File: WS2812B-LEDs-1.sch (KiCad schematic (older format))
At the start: 64 parts

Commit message: Getting lost in hirarchical schematic sheets...
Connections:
- net +5V renamed VCC

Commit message: Being creative...
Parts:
- C10, C11, C12, C13, C14, C15, C16, C17, C18, C19, C20, C21, C22, C23, C24, C25, C26, C27, C28, C29, C30, C31, C32, C33, C34, C35, C36, C5, C6, C7, C8, C9: footprint (none) -> my_parts:MADW__C0805
- LED1, LED10, LED11, LED12, LED13, LED14, LED15, LED16, LED17, LED18, LED19, LED2, LED20, LED21, LED22, LED23, LED24, LED25, LED26, LED27, LED28, LED29, LED3, LED30, LED31, LED32, LED4, LED5, LED6, LED7, LED8, LED9: footprint (none) -> WS2812B:WS2812B_data-bridgeable

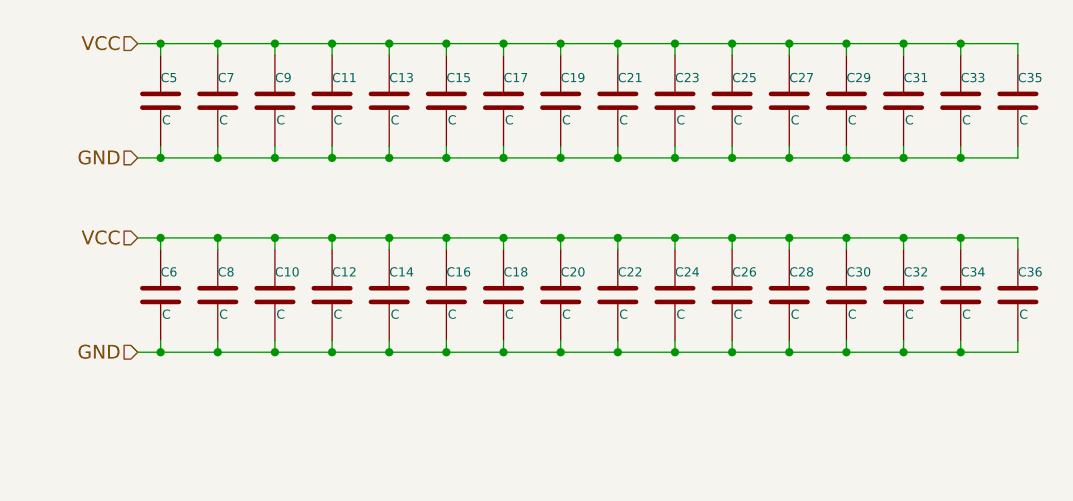
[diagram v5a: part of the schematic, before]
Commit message: Some cleanup. Still need to fix the power connector(s).
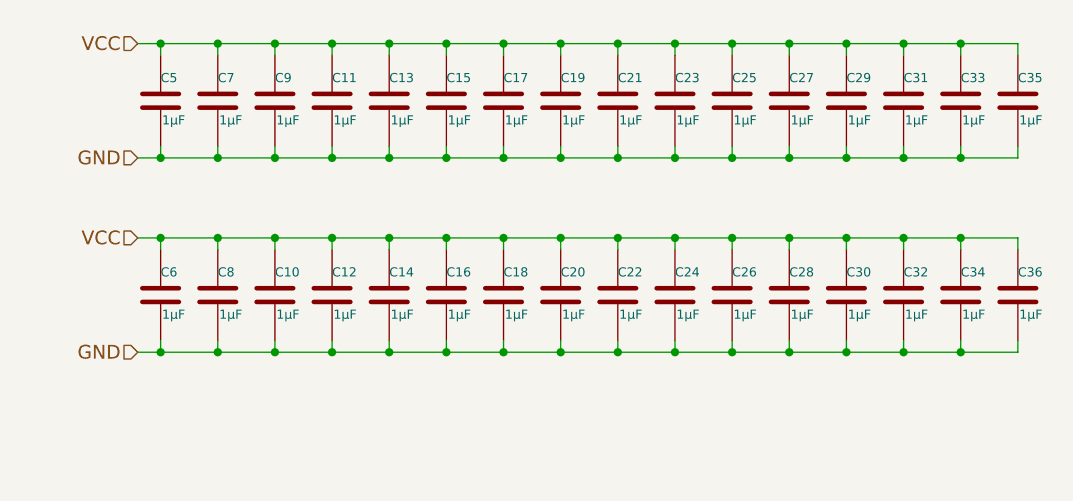
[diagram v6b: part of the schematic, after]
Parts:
- C10, C11, C12, C13, C14, C15, C16, C17, C18, C19, C20, C21, C22, C23, C24, C25, C26, C27, C28, C29, C30, C31, C32, C33, C34, C35, C36, C5, C6, C7, C8, C9: value C -> 1µF
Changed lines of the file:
@@
 P 7250 950
 F 0 "C5" H 7250 1050 40  0000 L CNN
-F 1 "C" H 7256 865 40  0000 L CNN
+F 1 "1µF" H 7256 865 40  0000 L CNN
 F 2 "my_parts:MADW__C0805" H 7288 800 30  0001 C CNN
 F 3 "" H 7250 950 60  0000 C CNN
@@
 P 7500 950
 F 0 "C7" H 7500 1050 40  0000 L CNN
-F 1 "C" H 7506 865 40  0000 L CNN
+F 1 "1µF" H 7506 865 40  0000 L CNN
 F 2 "my_parts:MADW__C0805" H 7538 800 30  0001 C CNN
 F 3 "" H 7500 950 60  0000 C CNN
@@
 P 7750 950
 F 0 "C9" H 7750 1050 40  0000 L CNN
-F 1 "C" H 7756 865 40  0000 L CNN
+F 1 "1µF" H 7756 865 40  0000 L CNN
 F 2 "my_parts:MADW__C0805" H 7788 800 30  0001 C CNN
 F 3 "" H 7750 950 60  0000 C CNN
@@
 P 8000 950
 F 0 "C11" H 8000 1050 40  0000 L CNN
-F 1 "C" H 8006 865 40  0000 L CNN
+F 1 "1µF" H 8006 865 40  0000 L CNN
 F 2 "my_parts:MADW__C0805" H 8038 800 30  0001 C CNN
 F 3 "" H 8000 950 60  0000 C CNN
@@
 P 8250 950
 F 0 "C13" H 8250 1050 40  0000 L CNN
-F 1 "C" H 8256 865 40  0000 L CNN
+F 1 "1µF" H 8256 865 40  0000 L CNN
 F 2 "my_parts:MADW__C0805" H 8288 800 30  0001 C CNN
 F 3 "" H 8250 950 60  0000 C CNN
@@
 P 8500 950
 F 0 "C15" H 8500 1050 40  0000 L CNN
-F 1 "C" H 8506 865 40  0000 L CNN
+F 1 "1µF" H 8506 865 40  0000 L CNN
 F 2 "my_parts:MADW__C0805" H 8538 800 30  0001 C CNN
 F 3 "" H 8500 950 60  0000 C CNN
@@
 P 8750 950
 F 0 "C17" H 8750 1050 40  0000 L CNN
-F 1 "C" H 8756 865 40  0000 L CNN
+F 1 "1µF" H 8756 865 40  0000 L CNN
 F 2 "my_parts:MADW__C0805" H 8788 800 30  0001 C CNN
 F 3 "" H 8750 950 60  0000 C CNN
@@
 P 9000 950
 F 0 "C19" H 9000 1050 40  0000 L CNN
-F 1 "C" H 9006 865 40  0000 L CNN
+F 1 "1µF" H 9006 865 40  0000 L CNN
 F 2 "my_parts:MADW__C0805" H 9038 800 30  0001 C CNN
 F 3 "" H 9000 950 60  0000 C CNN
@@
 P 9250 950
 F 0 "C21" H 9250 1050 40  0000 L CNN
-F 1 "C" H 9256 865 40  0000 L CNN
+F 1 "1µF" H 9256 865 40  0000 L CNN
 F 2 "my_parts:MADW__C0805" H 9288 800 30  0001 C CNN
 F 3 "" H 9250 950 60  0000 C CNN
@@
 P 9500 950
 F 0 "C23" H 9500 1050 40  0000 L CNN
-F 1 "C" H 9506 865 40  0000 L CNN
+F 1 "1µF" H 9506 865 40  0000 L CNN
 F 2 "my_parts:MADW__C0805" H 9538 800 30  0001 C CNN
 F 3 "" H 9500 950 60  0000 C CNN
@@
 P 9750 950
 F 0 "C25" H 9750 1050 40  0000 L CNN
-F 1 "C" H 9756 865 40  0000 L CNN
+F 1 "1µF" H 9756 865 40  0000 L CNN
 F 2 "my_parts:MADW__C0805" H 9788 800 30  0001 C CNN
 F 3 "" H 9750 950 60  0000 C CNN
@@
 P 10000 950
 F 0 "C27" H 10000 1050 40  0000 L CNN
-F 1 "C" H 10006 865 40  0000 L CNN
+F 1 "1µF" H 10006 865 40  0000 L CNN
 F 2 "my_parts:MADW__C0805" H 10038 800 30  0001 C CNN
 F 3 "" H 10000 950 60  0000 C CNN
@@
 P 10250 950
 F 0 "C29" H 10250 1050 40  0000 L CNN
-F 1 "C" H 10256 865 40  0000 L CNN
+F 1 "1µF" H 10256 865 40  0000 L CNN
 F 2 "my_parts:MADW__C0805" H 10288 800 30  0001 C CNN
 F 3 "" H 10250 950 60  0000 C CNN
@@
 P 10500 950
 F 0 "C31" H 10500 1050 40  0000 L CNN
-F 1 "C" H 10506 865 40  0000 L CNN
+F 1 "1µF" H 10506 865 40  0000 L CNN
 F 2 "my_parts:MADW__C0805" H 10538 800 30  0001 C CNN
 F 3 "" H 10500 950 60  0000 C CNN
@@
 P 10750 950
 F 0 "C33" H 10750 1050 40  0000 L CNN
-F 1 "C" H 10756 865 40  0000 L CNN
+F 1 "1µF" H 10756 865 40  0000 L CNN
 F 2 "my_parts:MADW__C0805" H 10788 800 30  0001 C CNN
 F 3 "" H 10750 950 60  0000 C CNN
@@
 P 11000 950
 F 0 "C35" H 11000 1050 40  0000 L CNN
-F 1 "C" H 11006 865 40  0000 L CNN
+F 1 "1µF" H 11006 865 40  0000 L CNN
 F 2 "my_parts:MADW__C0805" H 11038 800 30  0001 C CNN
 F 3 "" H 11000 950 60  0000 C CNN
@@
 P 7250 1800
 F 0 "C6" H 7250 1900 40  0000 L CNN
-F 1 "C" H 7256 1715 40  0000 L CNN
+F 1 "1µF" H 7256 1715 40  0000 L CNN
 F 2 "my_parts:MADW__C0805" H 7288 1650 30  0001 C CNN
 F 3 "" H 7250 1800 60  0000 C CNN
@@
 P 7500 1800
 F 0 "C8" H 7500 1900 40  0000 L CNN
-F 1 "C" H 7506 1715 40  0000 L CNN
+F 1 "1µF" H 7506 1715 40  0000 L CNN
 F 2 "my_parts:MADW__C0805" H 7538 1650 30  0001 C CNN
 F 3 "" H 7500 1800 60  0000 C CNN
@@
 P 7750 1800
 F 0 "C10" H 7750 1900 40  0000 L CNN
-F 1 "C" H 7756 1715 40  0000 L CNN
+F 1 "1µF" H 7756 1715 40  0000 L CNN
 F 2 "my_parts:MADW__C0805" H 7788 1650 30  0001 C CNN
 F 3 "" H 7750 1800 60  0000 C CNN
@@
 P 8000 1800
 F 0 "C12" H 8000 1900 40  0000 L CNN
-F 1 "C" H 8006 1715 40  0000 L CNN
+F 1 "1µF" H 8006 1715 40  0000 L CNN
 F 2 "my_parts:MADW__C0805" H 8038 1650 30  0001 C CNN
 F 3 "" H 8000 1800 60  0000 C CNN
@@
 P 8250 1800
 F 0 "C14" H 8250 1900 40  0000 L CNN
-F 1 "C" H 8256 1715 40  0000 L CNN
+F 1 "1µF" H 8256 1715 40  0000 L CNN
 F 2 "my_parts:MADW__C0805" H 8288 1650 30  0001 C CNN
 F 3 "" H 8250 1800 60  0000 C CNN
@@
 P 8500 1800
 F 0 "C16" H 8500 1900 40  0000 L CNN
-F 1 "C" H 8506 1715 40  0000 L CNN
+F 1 "1µF" H 8506 1715 40  0000 L CNN
 F 2 "my_parts:MADW__C0805" H 8538 1650 30  0001 C CNN
 F 3 "" H 8500 1800 60  0000 C CNN
@@
 P 8750 1800
 F 0 "C18" H 8750 1900 40  0000 L CNN
-F 1 "C" H 8756 1715 40  0000 L CNN
+F 1 "1µF" H 8756 1715 40  0000 L CNN
 F 2 "my_parts:MADW__C0805" H 8788 1650 30  0001 C CNN
 F 3 "" H 8750 1800 60  0000 C CNN
@@
 P 9000 1800
 F 0 "C20" H 9000 1900 40  0000 L CNN
-F 1 "C" H 9006 1715 40  0000 L CNN
+F 1 "1µF" H 9006 1715 40  0000 L CNN
 F 2 "my_parts:MADW__C0805" H 9038 1650 30  0001 C CNN
 F 3 "" H 9000 1800 60  0000 C CNN
@@
 P 9250 1800
 F 0 "C22" H 9250 1900 40  0000 L CNN
-F 1 "C" H 9256 1715 40  0000 L CNN
+F 1 "1µF" H 9256 1715 40  0000 L CNN
 F 2 "my_parts:MADW__C0805" H 9288 1650 30  0001 C CNN
 F 3 "" H 9250 1800 60  0000 C CNN
@@
 P 9500 1800
 F 0 "C24" H 9500 1900 40  0000 L CNN
-F 1 "C" H 9506 1715 40  0000 L CNN
+F 1 "1µF" H 9506 1715 40  0000 L CNN
 F 2 "my_parts:MADW__C0805" H 9538 1650 30  0001 C CNN
 F 3 "" H 9500 1800 60  0000 C CNN
@@
 P 9750 1800
 F 0 "C26" H 9750 1900 40  0000 L CNN
-F 1 "C" H 9756 1715 40  0000 L CNN
+F 1 "1µF" H 9756 1715 40  0000 L CNN
 F 2 "my_parts:MADW__C0805" H 9788 1650 30  0001 C CNN
 F 3 "" H 9750 1800 60  0000 C CNN
@@
 P 10000 1800
 F 0 "C28" H 10000 1900 40  0000 L CNN
-F 1 "C" H 10006 1715 40  0000 L CNN
+F 1 "1µF" H 10006 1715 40  0000 L CNN
 F 2 "my_parts:MADW__C0805" H 10038 1650 30  0001 C CNN
 F 3 "" H 10000 1800 60  0000 C CNN
@@
 P 10250 1800
 F 0 "C30" H 10250 1900 40  0000 L CNN
-F 1 "C" H 10256 1715 40  0000 L CNN
+F 1 "1µF" H 10256 1715 40  0000 L CNN
 F 2 "my_parts:MADW__C0805" H 10288 1650 30  0001 C CNN
 F 3 "" H 10250 1800 60  0000 C CNN
@@
 P 10500 1800
 F 0 "C32" H 10500 1900 40  0000 L CNN
-F 1 "C" H 10506 1715 40  0000 L CNN
+F 1 "1µF" H 10506 1715 40  0000 L CNN
 F 2 "my_parts:MADW__C0805" H 10538 1650 30  0001 C CNN
 F 3 "" H 10500 1800 60  0000 C CNN
@@
 P 10750 1800
 F 0 "C34" H 10750 1900 40  0000 L CNN
-F 1 "C" H 10756 1715 40  0000 L CNN
+F 1 "1µF" H 10756 1715 40  0000 L CNN
 F 2 "my_parts:MADW__C0805" H 10788 1650 30  0001 C CNN
 F 3 "" H 10750 1800 60  0000 C CNN
@@
 P 11000 1800
 F 0 "C36" H 11000 1900 40  0000 L CNN
-F 1 "C" H 11006 1715 40  0000 L CNN
+F 1 "1µF" H 11006 1715 40  0000 L CNN
 F 2 "my_parts:MADW__C0805" H 11038 1650 30  0001 C CNN
 F 3 "" H 11000 1800 60  0000 C CNN
